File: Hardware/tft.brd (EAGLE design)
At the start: 41.3 x 28.1 mm, 11 parts, among them J1 RJ45-8P8C, J2 40PINFPCM4-1734839-0

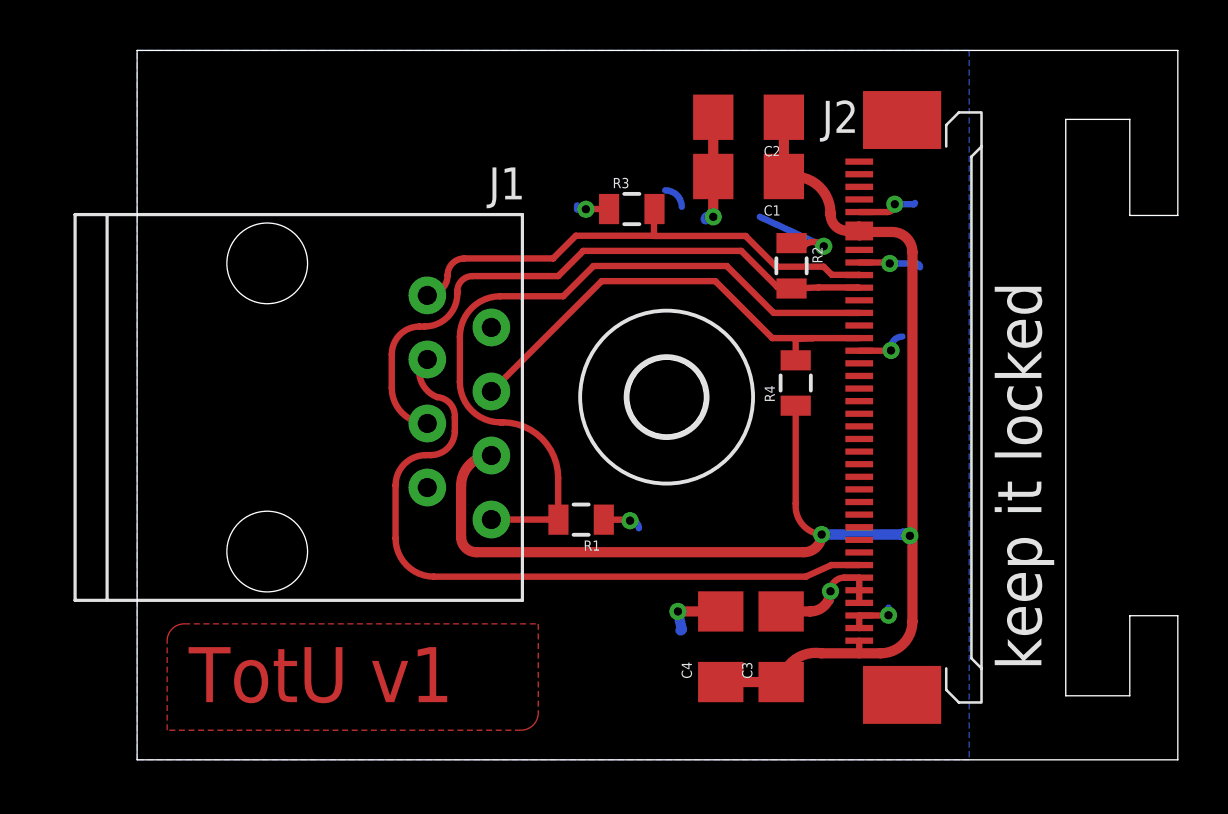
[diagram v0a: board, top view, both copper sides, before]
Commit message: Finished new tft board
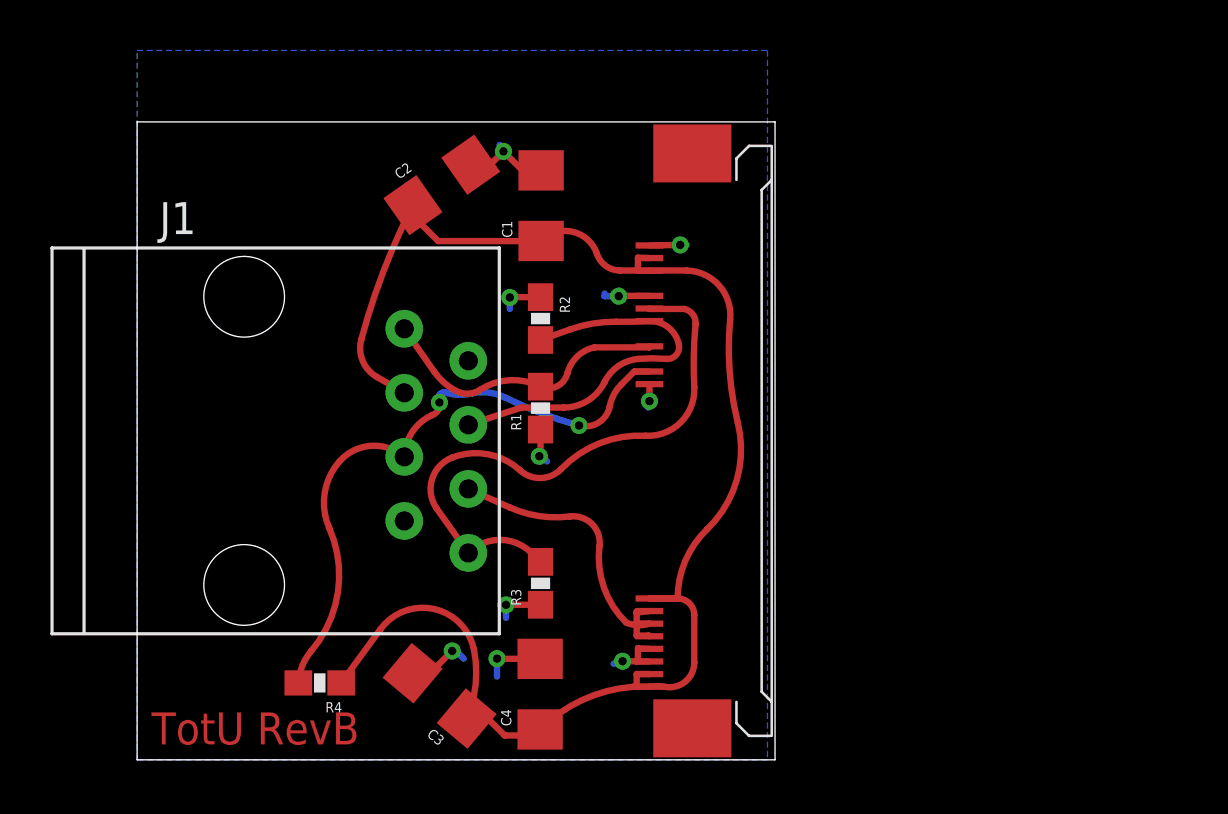
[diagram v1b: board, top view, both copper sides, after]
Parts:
- removed H1: MOUNT-HOLE3.0, holes:3,0
- removed J2: 40PINFPCM4-1734839-0, adafruit:4-1734839-0
- added U$1: XF2M-4015-WONKY, cape:XF2M-4015-WONKY
- R1, R2, R3, R4: device SparkFun-Passives:0805 -> SparkFun-Resistors:0603-RES
- moved R4 22.3 mm to (7.24, 3.05), turned to 180 degrees
- moved R3 15.3 mm to (16.0, 7.00), turned to 90 degrees
- moved C3 13.7 mm to (12.0, 2.54), turned to 140 degrees
- moved C2 12.5 mm to (12.1, 22.8), turned to 35 degrees
- moved R2 10.2 mm to (16.0, 17.5)
- moved C1 8.31 mm to (16.0, 22.0), turned to 90 degrees
- moved C4 7.41 mm to (16.0, 2.61)
- moved R1 4.71 mm to (16.0, 13.9), turned to 90 degrees
- moved J1 1.61 mm to (4.25, 12.7)
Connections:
- net BACKLIGHT: now also J1.6, U$1.34, U$1.35, U$1.36; no longer J1.3, J2.33
- net DATA: now also J1.1, U$1.13; no longer J1.8, J2.13
- net DC: now also J1.4, U$1.11; no longer J1.5, J2.11
- net GND: now also U$1.16, U$1.37, U$1.38, U$1.5, U$1.9; no longer J2.16, J2.34, J2.35, J2.36, J2.37, J2.38, J2.5, J2.9
- net RST: now also J1.5, U$1.15; no longer J1.4, J2.15
- net SCK: now also J1.8, U$1.10; no longer J1.1, J2.10
- net VCC3V3: now also J1.3, U$1.33, U$1.39, U$1.40, U$1.6, U$1.7; no longer J1.6, J2.39, J2.40, J2.6, J2.7
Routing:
- net DATA: track 29.4 -> 11.5 mm
- net BACKLIGHT: track 27.9 -> 12.5 mm
- net DC: track 24.8 -> 15.2 mm
- net GND: track 28.8 -> 20.3 mm
- net RST: track 18.9 -> 23.9 mm, vias 0 -> 2
- net SCK: track 19.8 -> 22.6 mm
- net VCC3V3: track 60.8 -> 61.6 mm, vias 2 -> 0
- removed copper zone on layer 1, net N$1
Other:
- board size 41.3 x 28.1 mm -> 25.3 x 25.3 mm
- board text added: "TotU RevB"
- board text removed: "TotU v1"
- board text removed: "keep it locked"
